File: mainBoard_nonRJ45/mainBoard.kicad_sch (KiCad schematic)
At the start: 45 parts, among them J1 XT60PW-M, J2 XT60PW-M, J21 B2B-PH_K, J22 Conn_01x02, J3 XT30PW-M, J4 XT30PW-M, J5 Barrel_Jack, J6 XT30U_M, Q1 FQD11P06TM, Q2 FQD11P06TM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

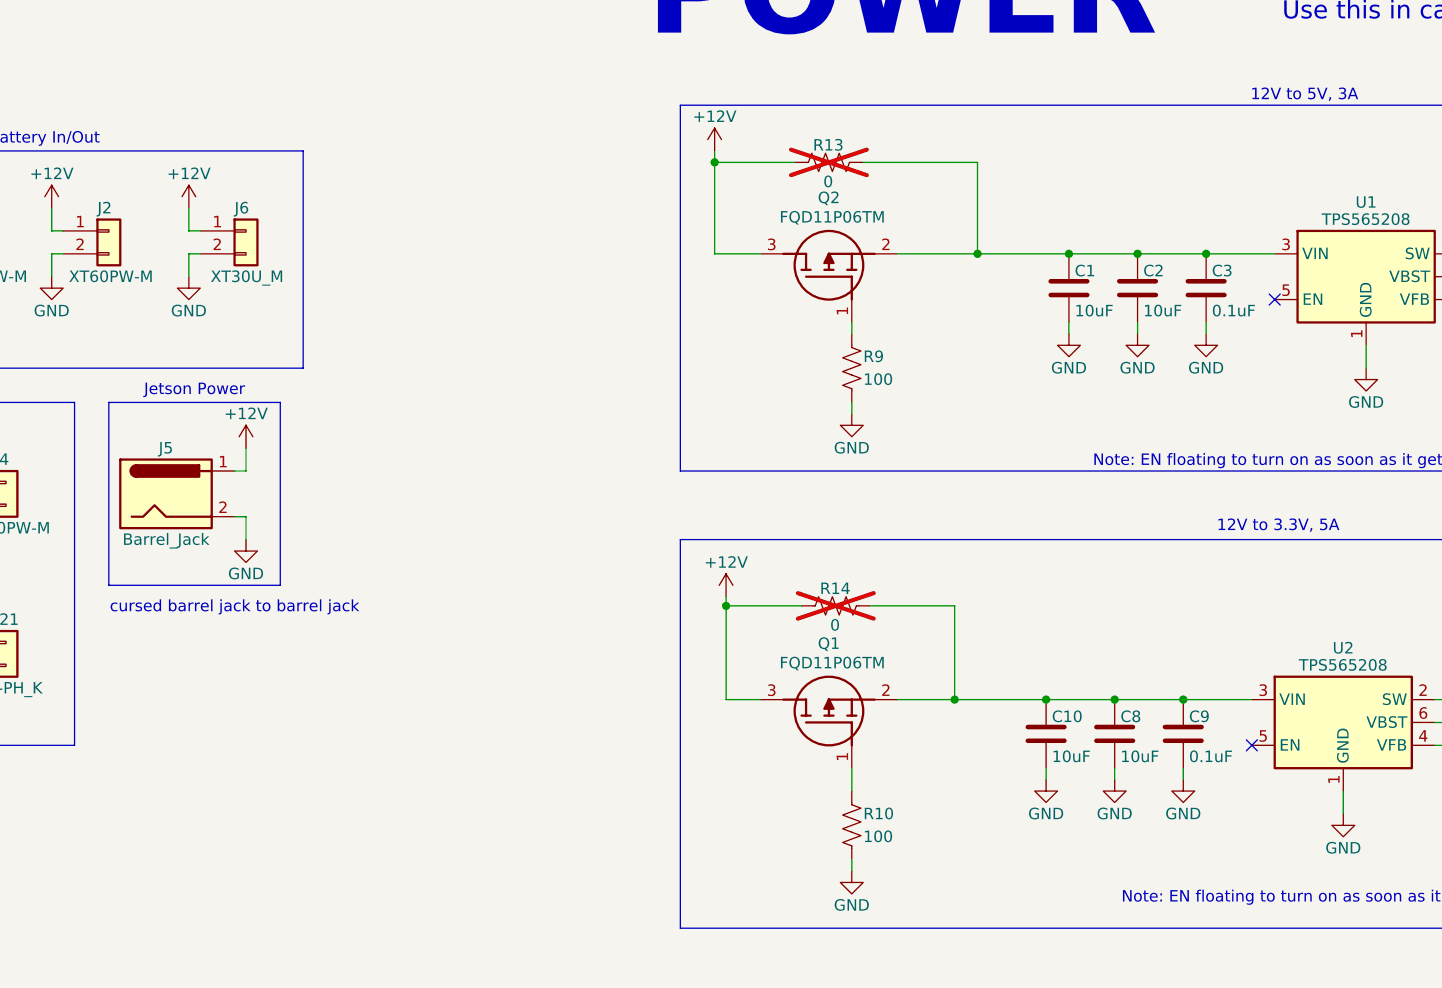
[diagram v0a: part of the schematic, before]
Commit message: Reviewed PCB with justin and made changes
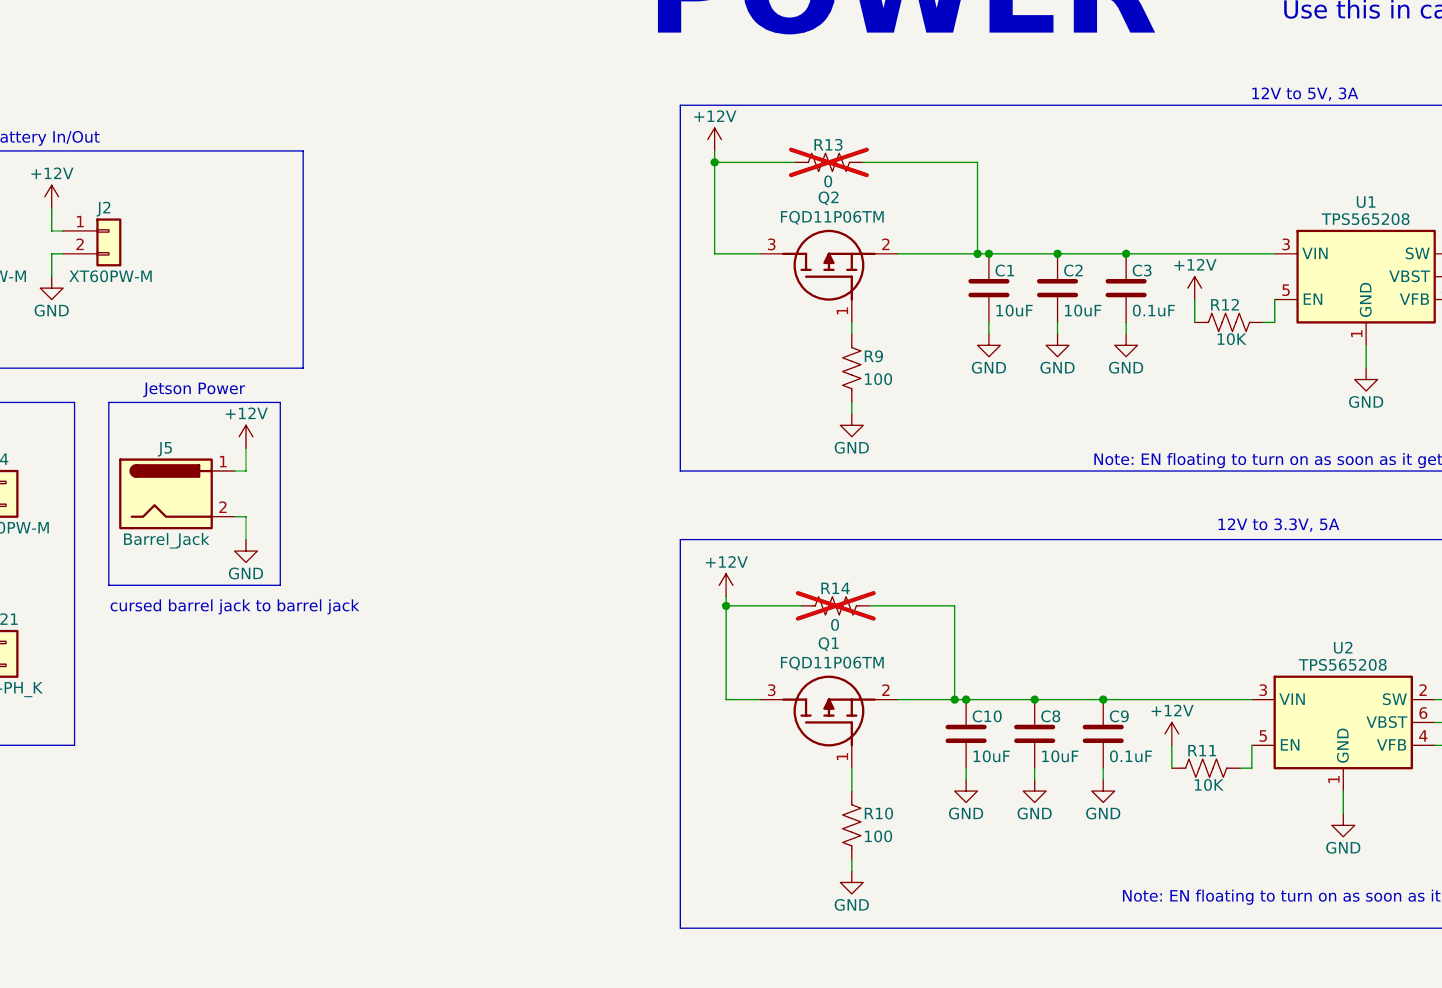
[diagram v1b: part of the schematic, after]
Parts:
- removed J6: XT30U_M, Connector_AMASS:AMASS_XT30U-M_1x02_P5.0mm_Vertical, symbol Connector_Generic:Conn_01x02
- added R11, R12: 10K, Resistor_SMD:R_0805_2012Metric_Pad1.20x1.40mm_HandSolder, symbol Device:R_US
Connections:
- net +12V: now also R11.1, R12.1
- net at U2.5 (EN): now also R11.2
- net at U1.5 (EN): now also R12.2
- no-connect marks 2 -> 0
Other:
- moved on the sheet: C1, C10, C2, C3, C8, C9

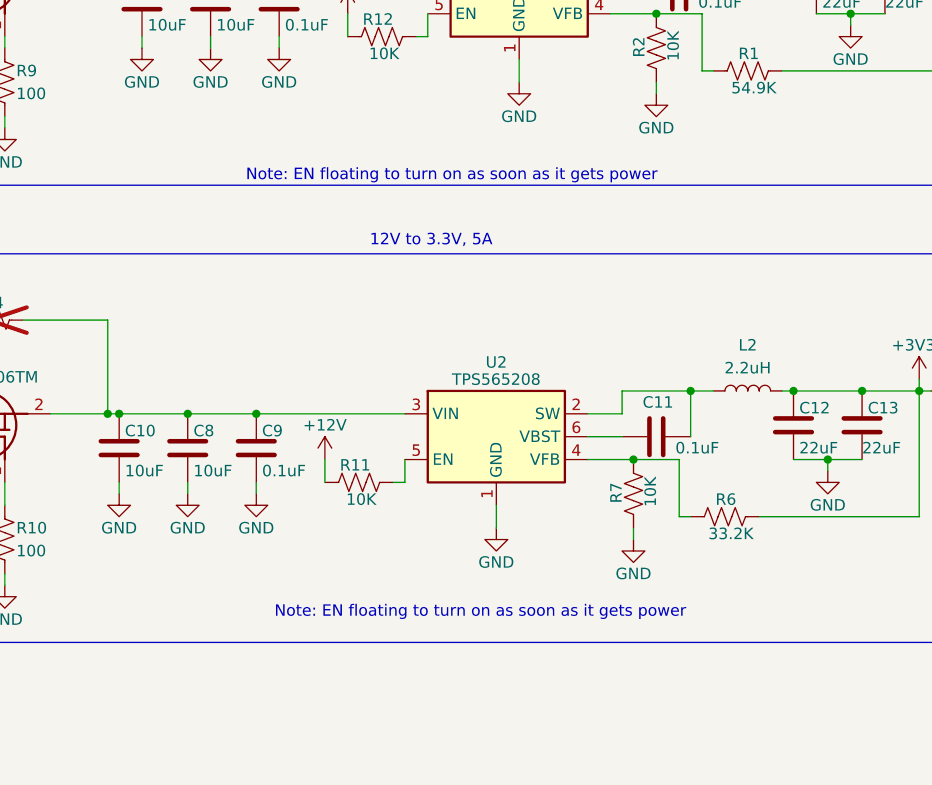
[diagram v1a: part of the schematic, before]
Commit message: create symbol and footprint for the Pololu 18v17 motor controller
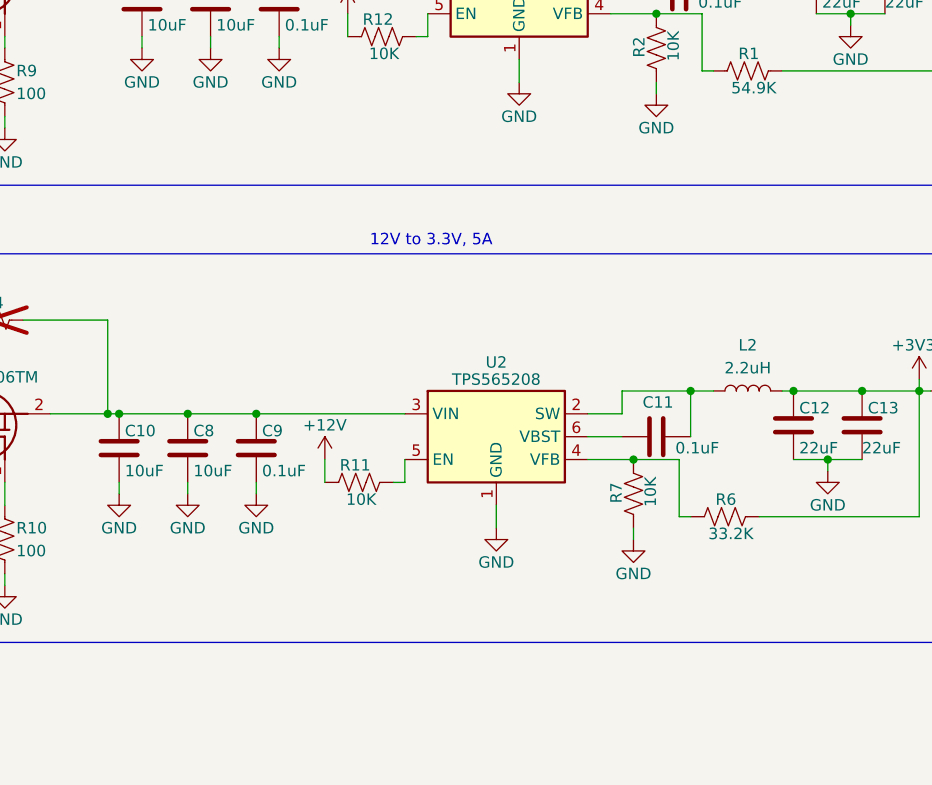
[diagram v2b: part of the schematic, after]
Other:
- note removed: "Note: EN floating to turn on as soon as it gets power"
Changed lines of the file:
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@@
-		)
-	)
-	(text "Note: EN floating to turn on as soon as it gets power"
-		(exclude_from_sim no)
-		(at 188.722 124.968 0)
-		(effects
-			(font
-				(size 1.27 1.27)
-			)
-		)
-	)
-	(text "Note: EN floating to turn on as soon as it gets power"
-		(exclude_from_sim no)
-		(at 185.547 76.454 0)
-		(effects
-			(font
-				(size 1.27 1.27)
-			)
 		)
 	)
